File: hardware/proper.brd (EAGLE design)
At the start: 68.6 x 50.5 mm, 42 parts, among them IC1 MEGA8-PU, IC3 MAX232, Q1 16MHz, T1 2N3904, T2 2N3904

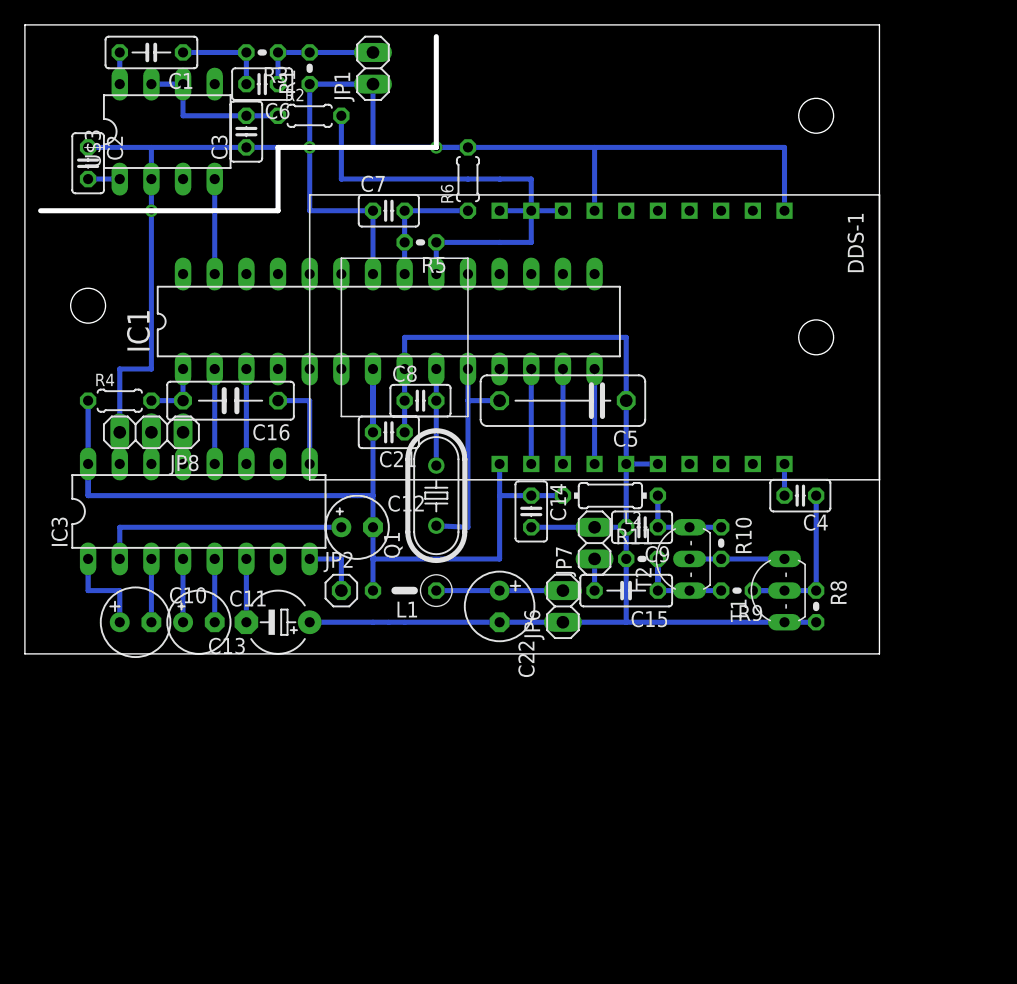
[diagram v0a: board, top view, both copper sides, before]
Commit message: Fixed minors, added win build.
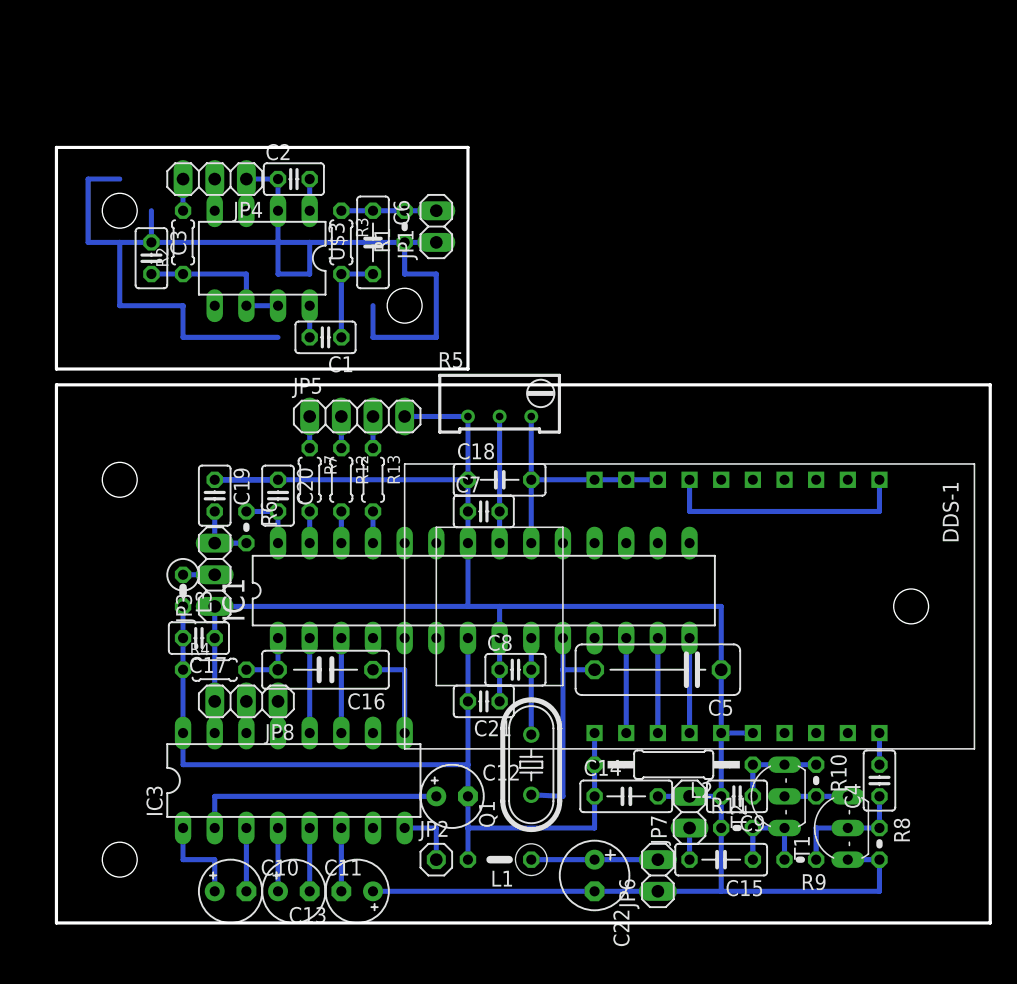
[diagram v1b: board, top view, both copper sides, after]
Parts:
- added C17: 10nF, rcl:C025-025X050
- added C18: 100nF, rcl:C050-025X075
- added C19, C20: 100nF, rcl:C025-025X050
- added JP3: Input, pinhead:1X03
- added JP4: Output, pinhead:1X03
- added JP5: LED, pinhead:1X04
- added L3: 100uH, rcl:0207/2V
- added R12, R13, R7: 1.5k, rcl:0204/5
- C1: device rcl:C050-025X075 -> rcl:C025-025X050
- C10: device rcl:E2,5-6 -> rcl:E2,5-5
- C13: device rcl:E5-5 -> rcl:E2,5-5
- C14, C6: device rcl:C025-025X050 -> rcl:C050-025X075
- JP1: value IN -> HF-IN
- JP7: value OUT -> HF-OUT
- L2: device rcl:0204/7 -> rcl:0207/12
- R3: device rcl:0204V -> rcl:0204/5
- R5: device rcl:0204V -> rcl:RTRIM64W
- R6: value 10k -> 2.2k; device rcl:0204/5 -> rcl:0204V
- moved R6 33.1 mm to (15.2, 31.8), turned to 270 degrees
- moved C1 26.8 mm to (21.6, 47.0)
- moved C7 25.3 mm to (34.3, 33.0)
- moved C14 24.1 mm to (45.7, 10.2), turned to 0 degrees
- moved C4 23.7 mm to (66.0, 11.4), turned to 90 degrees
- moved C15 22.9 mm to (53.3, 5.08)
- moved C10 22.9 mm to (14.0, 2.54)
- moved C11 22.9 mm to (19.1, 2.54)
- moved C12 22.9 mm to (31.8, 10.2)
- moved IC3 22.9 mm to (19.1, 11.4)
- moved JP2 22.9 mm to (30.5, 5.08)
- moved L1 22.9 mm to (35.6, 5.08)
- moved Q1 22.9 mm to (38.1, 12.7)
- moved C16 22.9 mm to (21.6, 20.3)
- moved C22 22.9 mm to (43.2, 3.81)
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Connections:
- new net +5V: JP4.3, R2.2
- new net N$14: C20.2, IC1.28, R6.1
- new net N$28: C7.2, IC1.21, R5.2
- new net N$30: JP5.1, R7.1
- new net N$31: JP5.2, R12.1
- new net N$32: JP5.3, R13.1
- new net N$33: C2.1, C3.1, JP1.1, JP4.1, R1.1, U$3.2
- new net N$35: IC1.27, R7.2
- new net N$36: IC1.26, R12.2
- new net N$37: IC1.25, R13.2
- new net N$42: C19.2, JP3.3, R6.2
- net GND: now also C17.1, C18.1, C19.1, C20.1, JP3.1, JP5.4, R5.1; no longer C2.1, C3.1, JP1.1, R1.1, R6.2, U$3.2
- net N$29: now also JP3.2, L3.1; no longer C7.2, IC1.21, R5.2, R6.1
- net N$9: now also JP4.2; no longer IC1.27
- net VCC: now also C17.2, C18.2, L3.2, R5.3; no longer R2.2, R5.1
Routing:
- net N$33: track 0.00 -> 91.4 mm
- net VCC: track 124.5 -> 91.4 mm
- net GND: track 226.1 -> 200.7 mm, vias 3 -> 0
- net N$28: track 0.00 -> 10.2 mm
- net N$29: track 10.2 -> 2.54 mm
- net N$42: track 0.00 -> 5.08 mm
- net N$14: track 0.00 -> 5.08 mm
- net N$9: track 7.62 -> 2.54 mm
- net N$13: track 15.2 -> 10.2 mm
- net N$21: track 7.62 -> 5.08 mm
- net N$24: track 10.2 -> 7.62 mm
- net N$37: track 0.00 -> 2.54 mm
- net N$36: track 0.00 -> 2.54 mm
- net N$35: track 0.00 -> 2.54 mm
- net N$32: track 0.00 -> 2.54 mm
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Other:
- board size 68.6 x 50.5 mm -> 74.9 x 62.2 mm

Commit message: Fixed minor.
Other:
- board size 74.9 x 62.2 mm -> 68.6 x 62.2 mm
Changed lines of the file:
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@@
 <hole x="5.08" y="5.08" drill="2.8"/>
 <wire x1="0" y1="0" x2="0" y2="43.18" width="0.254" layer="20"/>
-<wire x1="0" y1="43.18" x2="74.93" y2="43.18" width="0.254" layer="20"/>
-<wire x1="74.93" y1="43.18" x2="74.93" y2="0" width="0.254" layer="20"/>
-<wire x1="74.93" y1="0" x2="0" y2="0" width="0.254" layer="20"/>
+<wire x1="0" y1="43.18" x2="68.58" y2="43.18" width="0.254" layer="20"/>
+<wire x1="68.58" y1="43.18" x2="68.58" y2="0" width="0.254" layer="20"/>
+<wire x1="68.58" y1="0" x2="0" y2="0" width="0.254" layer="20"/>
 </plain>
 <attributes>
